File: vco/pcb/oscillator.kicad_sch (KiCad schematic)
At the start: 59 parts, among them Q2 BC847, SW2 SW_SPDT, U2 TL074, U3 LM13700, U4 ICM7555xB, U5 TL074

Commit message: vco: Layout
Silkscreen still needs adjustment.
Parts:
- removed R25, R30: 0R, Resistor_SMD:R_0603_1608Metric_Pad0.98x0.95mm_HandSolder, symbol Device:R
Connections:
- net GND: now also U5.5 (+); no longer U5.3 (+)
- net at SW2.2 (B), U3.5: now also U2.12 (+)
- net at R43.1, U2.10 (+), U2.14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: now also U2.13 (-)
- net at R43.2, R44.2, R46.1: now also U5.6 (-); no longer U5.13 (-)
- net at R35.2, R37.1, R38.2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: now also U3.10; no longer U3.7
- net at R47.2, U4.7 (DIS): now also U5.3 (+); no longer U5.5 (+)
- net at R49.1, R50.2, R53.1: now also U5.1; no longer U5.7
- net at R46.2, R47.1, R48.1: now also U5.7; no longer U5.14
- net at R39.2, U5.10 (+): now also U3.9; no longer U3.8
- net at R49.2, R51.1: now also U5.13 (-); no longer U5.2 (-)
- net at R51.2, R52.1: now also U5.14; no longer U5.1
- net at R48.2, R50.1: now also U5.2 (-); no longer U5.6 (-)
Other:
- moved on the sheet: U3B, U3D, U5A, U5B, U5D
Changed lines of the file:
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@@
-    (stroke (width 0) (type default) (color 0 0 0 0))
-  )
-  (wire (pts (xy 93.98 58.42) (xy 96.52 58.42))
     (stroke (width 0) (type default) (color 0 0 0 0))
   )
@@
     (stroke (width 0) (type default) (color 0 0 0 0))
   )
-  (wire (pts (xy 82.55 58.42) (xy 86.36 58.42))
+  (wire (pts (xy 82.55 58.42) (xy 96.52 58.42))
     (stroke (width 0) (type default) (color 0 0 0 0))
   )
@@
     (stroke (width 0) (type default) (color 0 0 0 0))
   )
-  (wire (pts (xy 107.95 74.93) (xy 115.57 74.93))
-    (stroke (width 0) (type default) (color 0 0 0 0))
-  )
   (wire (pts (xy 228.6 20.32) (xy 222.25 20.32))
     (stroke (width 0) (type default) (color 0 0 0 0))
@@
     (stroke (width 0) (type default) (color 0 0 0 0))
   )
+  (wire (pts (xy 93.98 74.93) (xy 115.57 74.93))
+    (stroke (width 0) (type default) (color 0 0 0 0))
+  )
   (wire (pts (xy 158.75 59.69) (xy 158.75 60.96))
     (stroke (width 0) (type default) (color 0 0 0 0))
@@
   )
   (wire (pts (xy 64.77 148.59) (xy 64.77 172.72))
-    (stroke (width 0) (type default) (color 0 0 0 0))
-  )
-  (wire (pts (xy 93.98 74.93) (xy 100.33 74.93))
     (stroke (width 0) (type default) (color 0 0 0 0))
   )
@@
       (effects (font (size 1.27 1.27)) (justify right) hide)
     )
-  )
-  (symbol (lib_id "Device:R") (at 90.17 58.42 90) (unit 1)
-    (in_bom yes) (on_board yes)
-    (property "Reference" "R25" (id 0) (at 90.17 52.07 90))
-    (property "Value" "0R" (id 1) (at 90.17 54.61 90))
-    (property "Footprint" "Resistor_SMD:R_0603_1608Metric_Pad0.98x0.95mm_HandSolder" (id 2) (at 90.17 60.198 90)
-      (effects (font (size 1.27 1.27)) hide)
-    )
-    (property "Datasheet" "~" (id 3) (at 90.17 58.42 0)
-      (effects (font (size 1.27 1.27)) hide)
-    )
-    (pin "1")
-    (pin "2")
   )
   (symbol (lib_id "Device:R") (at 189.23 63.5 90) (unit 1)
@@
     (pin "2")
   )
-  (symbol (lib_id "Amplifier_Operational:TL074") (at 213.36 64.77 0) (unit 4)
-    (in_bom yes) (on_board yes) (fields_autoplaced)
-    (property "Reference" "U5" (id 0) (at 213.36 54.61 0))
-    (property "Value" "TL074" (id 1) (at 213.36 57.15 0))
-    (property "Footprint" "Package_SO:SOIC-14_3.9x8.7mm_P1.27mm" (id 2) (at 212.09 62.23 0)
-      (effects (font (size 1.27 1.27)) hide)
-    )
-    (property "Datasheet" "http://www.ti.com/lit/ds/symlink/tl071.pdf" (id 3) (at 214.63 59.69 0)
+  (symbol (lib_id "Amplifier_Operational:TL074") (at 251.46 105.41 0) (unit 4)
+    (in_bom yes) (on_board yes) (fields_autoplaced)
+    (property "Reference" "U5" (id 0) (at 251.46 95.25 0))
+    (property "Value" "TL074" (id 1) (at 251.46 97.79 0))
+    (property "Footprint" "Package_SO:SOIC-14_3.9x8.7mm_P1.27mm" (id 2) (at 250.19 102.87 0)
+      (effects (font (size 1.27 1.27)) hide)
+    )
+    (property "Datasheet" "http://www.ti.com/lit/ds/symlink/tl071.pdf" (id 3) (at 252.73 100.33 0)
       (effects (font (size 1.27 1.27)) hide)
     )
@@
     (pin "2")
   )
-  (symbol (lib_id "Amplifier_Operational:TL074") (at 251.46 105.41 0) (unit 1)
-    (in_bom yes) (on_board yes) (fields_autoplaced)
-    (property "Reference" "U5" (id 0) (at 251.46 95.25 0))
-    (property "Value" "TL074" (id 1) (at 251.46 97.79 0))
-    (property "Footprint" "Package_SO:SOIC-14_3.9x8.7mm_P1.27mm" (id 2) (at 250.19 102.87 0)
-      (effects (font (size 1.27 1.27)) hide)
-    )
-    (property "Datasheet" "http://www.ti.com/lit/ds/symlink/tl071.pdf" (id 3) (at 252.73 100.33 0)
+  (symbol (lib_id "Amplifier_Operational:TL074") (at 251.46 64.77 0) (unit 1)
+    (in_bom yes) (on_board yes) (fields_autoplaced)
+    (property "Reference" "U5" (id 0) (at 251.46 54.61 0))
+    (property "Value" "TL074" (id 1) (at 251.46 57.15 0))
+    (property "Footprint" "Package_SO:SOIC-14_3.9x8.7mm_P1.27mm" (id 2) (at 250.19 62.23 0)
+      (effects (font (size 1.27 1.27)) hide)
+    )
+    (property "Datasheet" "http://www.ti.com/lit/ds/symlink/tl071.pdf" (id 3) (at 252.73 59.69 0)
       (effects (font (size 1.27 1.27)) hide)
     )
@@
     (pin "2")
   )
-  (symbol (lib_id "Device:R") (at 104.14 74.93 90) (unit 1)
-    (in_bom yes) (on_board yes) (fields_autoplaced)
-    (property "Reference" "R30" (id 0) (at 104.14 68.58 90))
-    (property "Value" "0R" (id 1) (at 104.14 71.12 90))
-    (property "Footprint" "Resistor_SMD:R_0603_1608Metric_Pad0.98x0.95mm_HandSolder" (id 2) (at 104.14 76.708 90)
-      (effects (font (size 1.27 1.27)) hide)
-    )
-    (property "Datasheet" "~" (id 3) (at 104.14 74.93 0)
-      (effects (font (size 1.27 1.27)) hide)
-    )
-    (pin "1")
-    (pin "2")
-  )
   (symbol (lib_id "Device:C") (at 76.2 69.85 180) (unit 1)
     (in_bom yes) (on_board yes)
@@
     (pin "1")
   )
-  (symbol (lib_id "Amplifier_Operational:LM13700") (at 52.07 68.58 0) (unit 2)
-    (in_bom yes) (on_board yes) (fields_autoplaced)
-    (property "Reference" "U3" (id 0) (at 49.53 58.42 0))
-    (property "Value" "LM13700" (id 1) (at 49.53 60.96 0))
-    (property "Footprint" "Package_SO:SOIC-16_3.9x9.9mm_P1.27mm" (id 2) (at 44.45 67.945 0)
-      (effects (font (size 1.27 1.27)) hide)
-    )
-    (property "Datasheet" "http://www.ti.com/lit/ds/symlink/lm13700.pdf" (id 3) (at 44.45 67.945 0)
+  (symbol (lib_id "Amplifier_Operational:LM13700") (at 153.67 120.65 0) (unit 2)
+    (in_bom yes) (on_board yes) (fields_autoplaced)
+    (property "Reference" "U3" (id 0) (at 151.13 110.49 0))
+    (property "Value" "LM13700" (id 1) (at 151.13 113.03 0))
+    (property "Footprint" "Package_SO:SOIC-16_3.9x9.9mm_P1.27mm" (id 2) (at 146.05 120.015 0)
+      (effects (font (size 1.27 1.27)) hide)
+    )
+    (property "Datasheet" "http://www.ti.com/lit/ds/symlink/lm13700.pdf" (id 3) (at 146.05 120.015 0)
       (effects (font (size 1.27 1.27)) hide)
     )
@@
     (pin "2")
   )
-  (symbol (lib_id "Amplifier_Operational:LM13700") (at 153.67 120.65 0) (unit 4)
-    (in_bom yes) (on_board yes) (fields_autoplaced)
-    (property "Reference" "U3" (id 0) (at 151.13 110.49 0))
-    (property "Value" "LM13700" (id 1) (at 151.13 113.03 0))
-    (property "Footprint" "Package_SO:SOIC-16_3.9x9.9mm_P1.27mm" (id 2) (at 146.05 120.015 0)
-      (effects (font (size 1.27 1.27)) hide)
-    )
-    (property "Datasheet" "http://www.ti.com/lit/ds/symlink/lm13700.pdf" (id 3) (at 146.05 120.015 0)
+  (symbol (lib_id "Amplifier_Operational:LM13700") (at 52.07 68.58 0) (unit 4)
+    (in_bom yes) (on_board yes) (fields_autoplaced)
+    (property "Reference" "U3" (id 0) (at 49.53 58.42 0))
+    (property "Value" "LM13700" (id 1) (at 49.53 60.96 0))
+    (property "Footprint" "Package_SO:SOIC-16_3.9x9.9mm_P1.27mm" (id 2) (at 44.45 67.945 0)
+      (effects (font (size 1.27 1.27)) hide)
+    )
+    (property "Datasheet" "http://www.ti.com/lit/ds/symlink/lm13700.pdf" (id 3) (at 44.45 67.945 0)
       (effects (font (size 1.27 1.27)) hide)
     )
@@
     (pin "2")
   )
-  (symbol (lib_id "Amplifier_Operational:TL074") (at 251.46 64.77 0) (unit 2)
-    (in_bom yes) (on_board yes) (fields_autoplaced)
-    (property "Reference" "U5" (id 0) (at 251.46 54.61 0))
-    (property "Value" "TL074" (id 1) (at 251.46 57.15 0))
-    (property "Footprint" "Package_SO:SOIC-14_3.9x8.7mm_P1.27mm" (id 2) (at 250.19 62.23 0)
-      (effects (font (size 1.27 1.27)) hide)
-    )
-    (property "Datasheet" "http://www.ti.com/lit/ds/symlink/tl071.pdf" (id 3) (at 252.73 59.69 0)
-      (effects (font (size 1.27 1.27)) hide)
-    )
+  (symbol (lib_id "Amplifier_Operational:TL074") (at 213.36 64.77 0) (unit 2)
+    (in_bom yes) (on_board yes) (fields_autoplaced)
+    (property "Reference" "U5" (id 0) (at 213.36 54.61 0))
+    (property "Value" "TL074" (id 1) (at 213.36 57.15 0))
+    (property "Footprint" "Package_SO:SOIC-14_3.9x8.7mm_P1.27mm" (id 2) (at 212.09 62.23 0)
+      (effects (font (size 1.27 1.27)) hide)
+    )
+    (property "Datasheet" "http://www.ti.com/lit/ds/symlink/tl071.pdf" (id 3) (at 214.63 59.69 0)
+      (effects (font (size 1.27 1.27)) hide)
+    )

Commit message: vco: Add Mouser order codes
Add Mouser order codes to some parts.  THis solution isn't really nice, though.
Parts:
- D4: Mouser (none) -> 604-WP424IDT
- Q2: Mouser (none) -> 771-BC847C-T/R
- U2, U5: Mouser (none) -> 595-TL074CDR
- U3: Mouser (none) -> 926-LM13700MX/NOPB
- U4: Mouser (none) -> 968-ICM7555IBAZ-T
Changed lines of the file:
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@@
+      (effects (font (size 1.27 1.27)) hide)
+    )
+    (property "Mouser" " 968-ICM7555IBAZ-T " (id 4) (at 158.75 49.53 0)
       (effects (font (size 1.27 1.27)) hide)
     )
@@
     )
     (property "Datasheet" "http://www.ti.com/lit/ds/symlink/lm13700.pdf" (id 3) (at 41.91 51.435 0)
+      (effects (font (size 1.27 1.27)) hide)
+    )
+    (property "Mouser" " 926-LM13700MX/NOPB " (id 4) (at 49.53 50.8 0)
       (effects (font (size 1.27 1.27)) hide)
     )
@@
     )
     (property "Datasheet" "http://www.ti.com/lit/ds/symlink/tl071.pdf" (id 3) (at 52.07 170.18 0)
+      (effects (font (size 1.27 1.27)) hide)
+    )
+    (property "Mouser" " 595-TL074CDR " (id 4) (at 50.8 175.26 0)
       (effects (font (size 1.27 1.27)) hide)
     )
@@
       (effects (font (size 1.27 1.27)) (justify left) hide)
     )
+    (property "Mouser" " 771-BC847C-T/R " (id 4) (at 114.3 41.275 0)
+      (effects (font (size 1.27 1.27)) hide)
+    )
     (pin "1")
     (pin "2")
@@
     )
     (property "Datasheet" "http://www.ti.com/lit/ds/symlink/lm13700.pdf" (id 3) (at 113.03 121.285 0)
+      (effects (font (size 1.27 1.27)) hide)
+    )
+    (property "Mouser" " 926-LM13700MX/NOPB " (id 4) (at 120.65 120.65 0)
       (effects (font (size 1.27 1.27)) hide)
     )
@@
       (effects (font (size 1.27 1.27)) hide)
     )
+    (property "Mouser" " 926-LM13700MX/NOPB " (id 4) (at 191.77 29.21 0)
+      (effects (font (size 1.27 1.27)) hide)
+    )
     (pin "12")
     (pin "13")
@@
     )
     (property "Datasheet" "http://www.ti.com/lit/ds/symlink/tl071.pdf" (id 3) (at 189.23 101.6 0)
+      (effects (font (size 1.27 1.27)) hide)
+    )
+    (property "Mouser" " 595-TL074CDR " (id 4) (at 187.96 106.68 0)
       (effects (font (size 1.27 1.27)) hide)
     )
@@
       (effects (font (size 1.27 1.27)) hide)
     )
+    (property "Mouser" " 595-TL074CDR " (id 4) (at 243.84 29.21 0)
+      (effects (font (size 1.27 1.27)) hide)
+    )
     (pin "1")
     (pin "2")
@@
       (effects (font (size 1.27 1.27)) hide)
     )
+    (property "Mouser" " 595-TL074CDR " (id 4) (at 251.46 105.41 0)
+      (effects (font (size 1.27 1.27)) hide)
+    )
     (pin "1")
     (pin "2")
@@
       (effects (font (size 1.27 1.27)) hide)
     )
+    (property "Mouser" " 604-WP424IDT " (id 4) (at 137.16 165.1 0)
+      (effects (font (size 1.27 1.27)) hide)
+    )
     (pin "1")
     (pin "2")
@@
     )
     (property "Datasheet" "http://www.ti.com/lit/ds/symlink/tl071.pdf" (id 3) (at 252.73 59.69 0)
+      (effects (font (size 1.27 1.27)) hide)
+    )
+    (property "Mouser" " 595-TL074CDR " (id 4) (at 251.46 64.77 0)
       (effects (font (size 1.27 1.27)) hide)
     )
@@
       (effects (font (size 1.27 1.27)) hide)
     )
+    (property "Mouser" " 926-LM13700MX/NOPB " (id 4) (at 153.67 120.65 0)
+      (effects (font (size 1.27 1.27)) hide)
+    )
     (pin "12")
     (pin "13")
@@
       (effects (font (size 1.27 1.27)) hide)
     )
+    (property "Mouser" " 926-LM13700MX/NOPB " (id 4) (at 52.07 68.58 0)
+      (effects (font (size 1.27 1.27)) hide)
+    )
     (pin "12")
     (pin "13")
@@
     )
     (property "Datasheet" "http://www.ti.com/lit/ds/symlink/tl071.pdf" (id 3) (at 214.63 59.69 0)
+      (effects (font (size 1.27 1.27)) hide)
+    )
+    (property "Mouser" " 595-TL074CDR " (id 4) (at 213.36 64.77 0)
       (effects (font (size 1.27 1.27)) hide)
     )
@@
       (effects (font (size 1.27 1.27)) hide)
     )
+    (property "Mouser" " 595-TL074CDR " (id 4) (at 87.63 175.26 0)
+      (effects (font (size 1.27 1.27)) hide)
+    )
     (pin "1")
     (pin "2")
@@
       (effects (font (size 1.27 1.27)) hide)
     )
+    (property "Mouser" " 595-TL074CDR " (id 4) (at 36.83 107.95 0)
+      (effects (font (size 1.27 1.27)) hide)
+    )
     (pin "1")
     (pin "2")
@@
       (effects (font (size 1.27 1.27)) hide)
     )
+    (property "Mouser" " 595-TL074CDR " (id 4) (at 104.14 60.96 0)
+      (effects (font (size 1.27 1.27)) hide)
+    )
     (pin "1")
     (pin "2")
@@
       (effects (font (size 1.27 1.27)) hide)
     )
+    (property "Mouser" " 595-TL074CDR " (id 4) (at 218.44 29.21 0)
+      (effects (font (size 1.27 1.27)) hide)
+    )

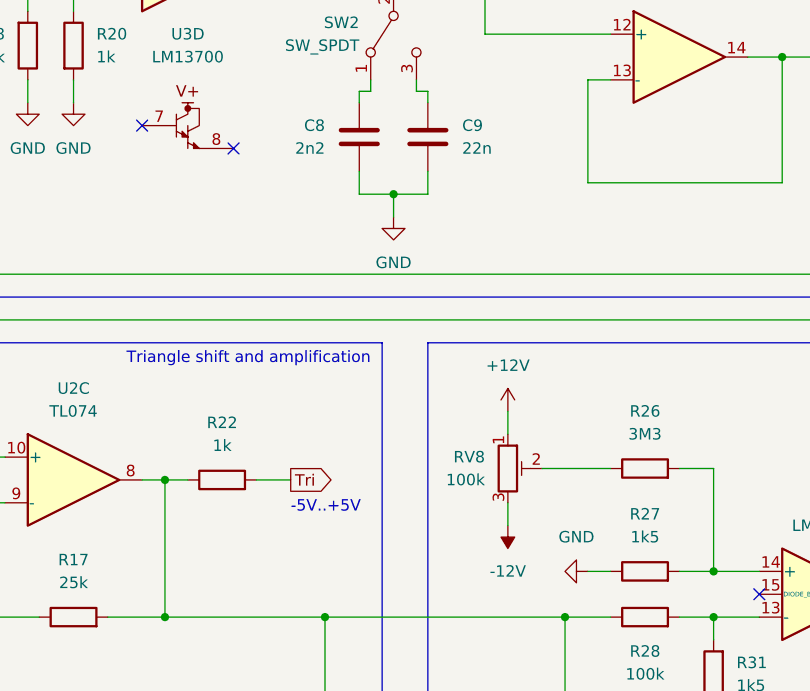
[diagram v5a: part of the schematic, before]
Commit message: vco: Add more info to silk
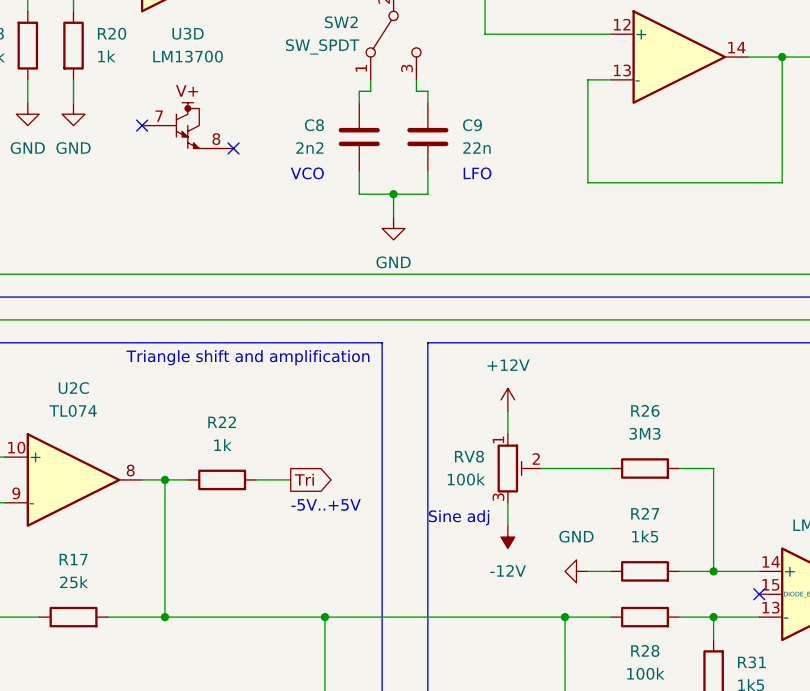
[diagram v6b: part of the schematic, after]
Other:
- note added: "LFO"
- note added: "Sine adj"
- note added: "VCO"
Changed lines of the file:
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@@
+    (effects (font (size 1.27 1.27)) (justify left bottom))
+  )
+  (text "Sine adj" (at 76.2 113.03 0)
     (effects (font (size 1.27 1.27)) (justify left bottom))
   )
@@
     (effects (font (size 1.27 1.27)) (justify left bottom))
   )
+  (text "VCO" (at 60.96 74.93 0)
+    (effects (font (size 1.27 1.27)) (justify left bottom))
+  )
+  (text "LFO" (at 80.01 74.93 0)
+    (effects (font (size 1.27 1.27)) (justify left bottom))
+  )

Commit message: vco: Update headers in pcb
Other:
- company: (none) -> L. Rittel
- title: Oscillator -> (VC|LF)O Oscillator
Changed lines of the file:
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@@
   (paper "A4")
   (title_block
-    (title "Oscillator")
-    (date "2022-12-30")
-    (rev "Rev. 1")
+    (title "(VC|LF)O Oscillator")
+    (date "2022-12-31")
+    (rev "Rev. 1 2022")
+    (company "L. Rittel")
   )
   (junction (at 247.65 38.1) (diameter 0) (color 0 0 0 0)

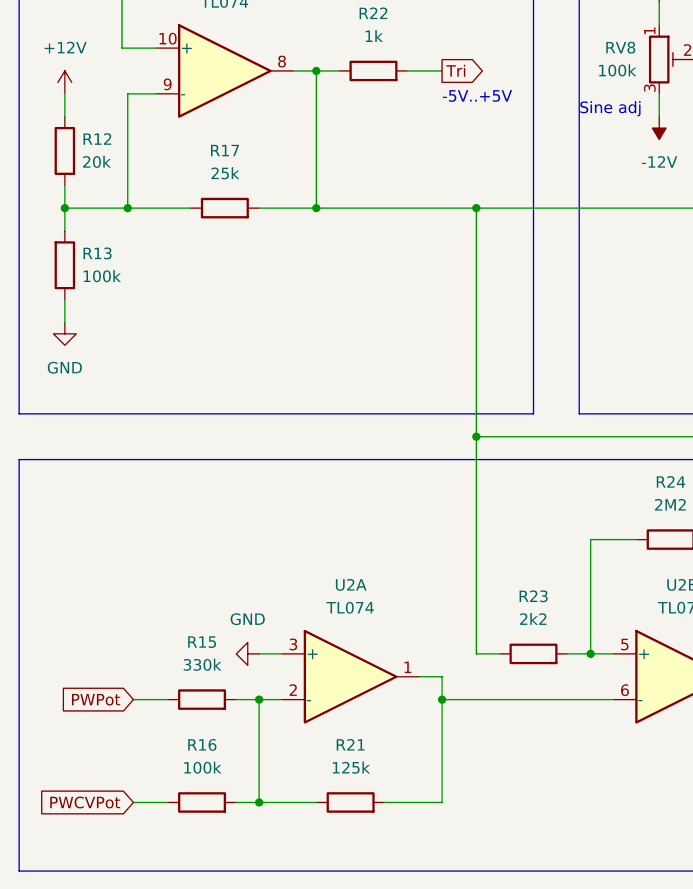
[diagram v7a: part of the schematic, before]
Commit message: vco: Change some resistors to Exx values
Some values didn't exist in any of ≤E96.
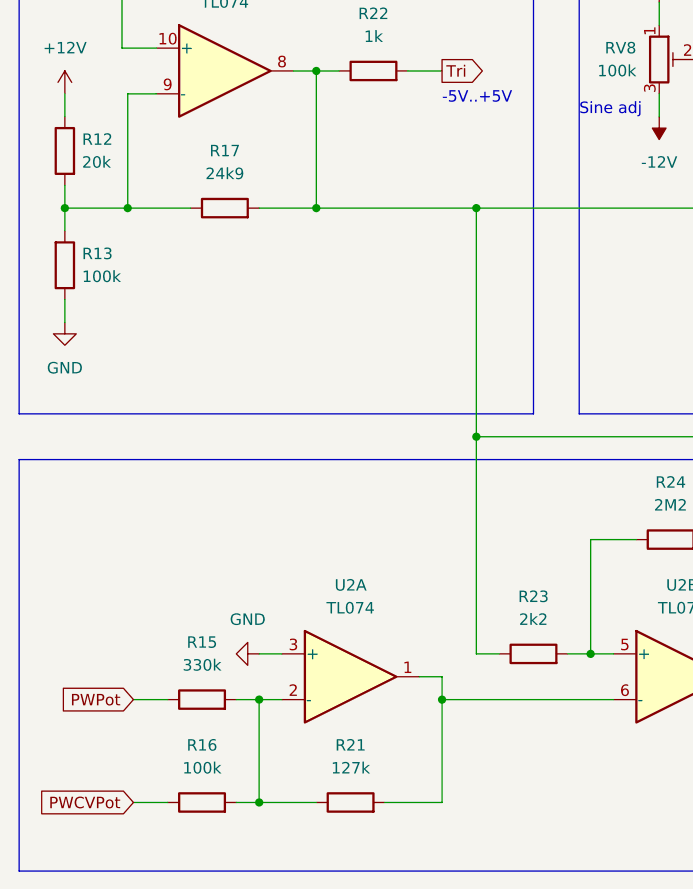
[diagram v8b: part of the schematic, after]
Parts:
- R17: value 25k -> 24k9
- R21: value 125k -> 127k
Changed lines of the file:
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@@
     (in_bom yes) (on_board yes) (fields_autoplaced)
     (property "Reference" "R17" (id 0) (at 36.83 116.84 90))
-    (property "Value" "25k" (id 1) (at 36.83 119.38 90))
+    (property "Value" "24k9" (id 1) (at 36.83 119.38 90))
     (property "Footprint" "Resistor_SMD:R_0603_1608Metric_Pad0.98x0.95mm_HandSolder" (id 2) (at 36.83 124.968 90)
       (effects (font (size 1.27 1.27)) hide)
@@
     (in_bom yes) (on_board yes) (fields_autoplaced)
     (property "Reference" "R21" (id 0) (at 50.8 182.88 90))
-    (property "Value" "125k" (id 1) (at 50.8 185.42 90))
+    (property "Value" "127k" (id 1) (at 50.8 185.42 90))
     (property "Footprint" "Resistor_SMD:R_0603_1608Metric_Pad0.98x0.95mm_HandSolder" (id 2) (at 50.8 191.008 90)
       (effects (font (size 1.27 1.27)) hide)
